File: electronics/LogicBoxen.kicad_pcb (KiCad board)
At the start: 2 copper layers, 50 x 35 mm, 47 parts, among them P1 Input, P2 Output, P3 Power, P4 L2, P5 L1, P6 OUT, Q1 Q_NMOS_DGS, SW1 DIPS_04, U1 4015, U2 4050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

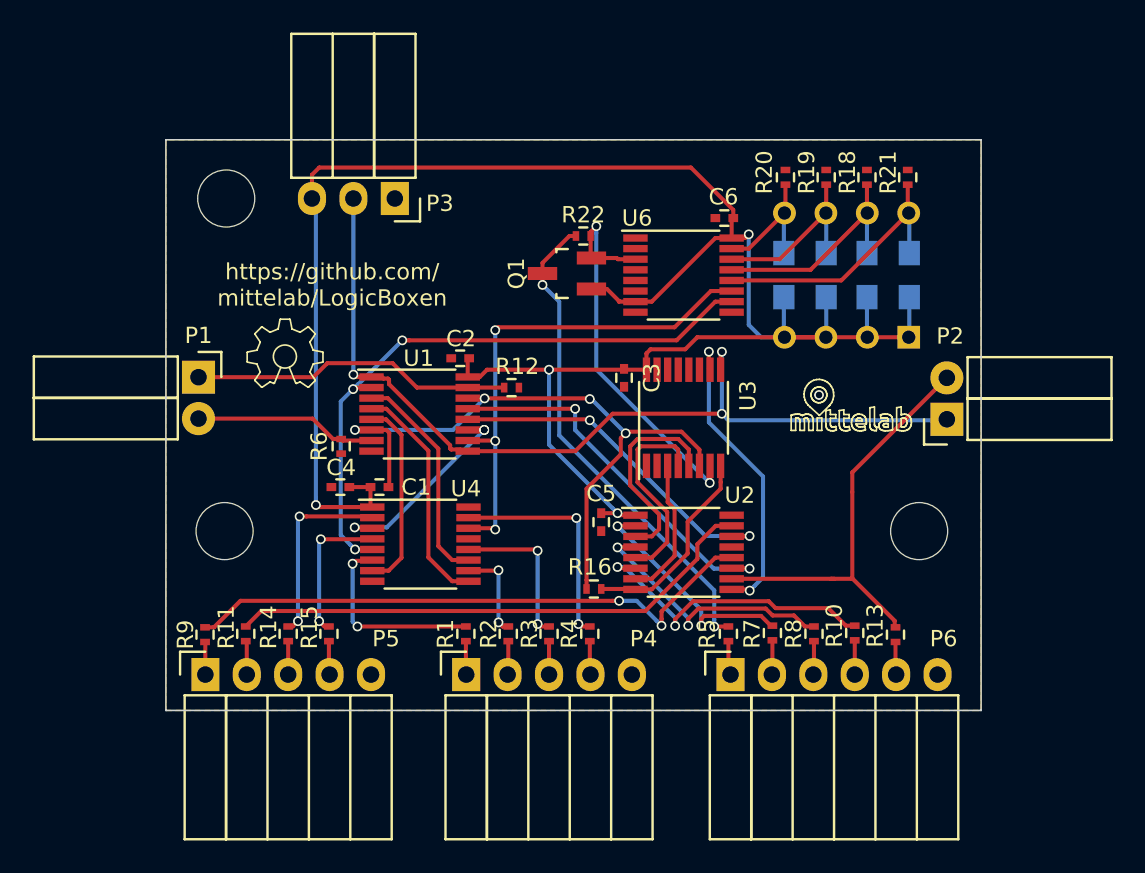
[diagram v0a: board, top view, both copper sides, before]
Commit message: Move vias away from pads, rearrange some tracks
Move R16 to a better place
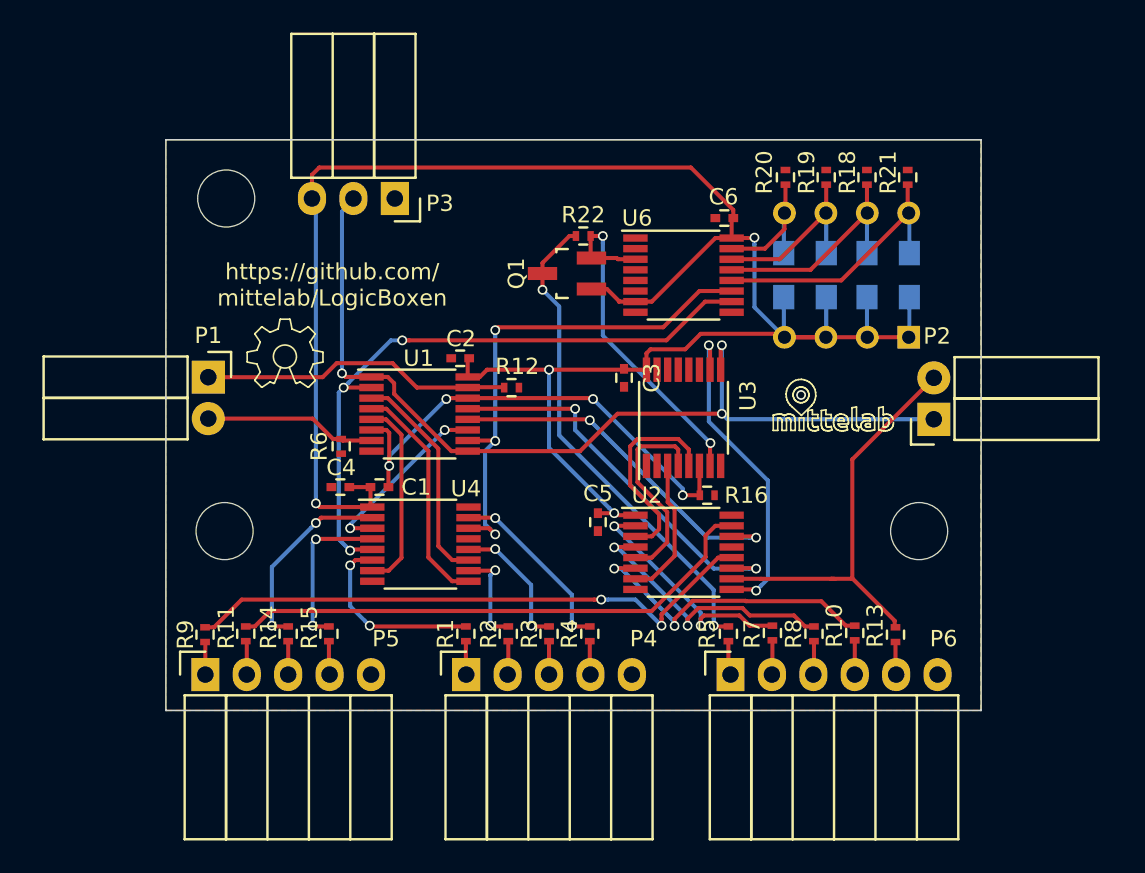
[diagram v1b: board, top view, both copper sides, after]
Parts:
- moved R16 9.02 mm to (57.2, 50.5)
- moved P2 0.80 mm to (71.1, 45.8)
- moved P1 0.60 mm to (26.6, 43.3)
- moved C5 0.20 mm to (50.5, 52.1)
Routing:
- net VSS: track 12.4 -> 0.06 mm
- net /reset: track 42.6 -> 30.3 mm
- net /out: track 24.6 -> 21.8 mm
- net Net-(R4-Pad1): track 13.9 -> 11.3 mm
- net /in_b: track 38.3 -> 39.6 mm
- net Net-(U2-Pad9): track 18.7 -> 19.9 mm
- net Net-(R3-Pad1): track 9.53 -> 8.38 mm
- net Net-(U1-Pad11): track 12.3 -> 11.2 mm, vias 3 -> 2
- net /clock: track 56.1 -> 57.1 mm
- net /in_a: track 31.1 -> 32.0 mm
- net Net-(R15-Pad1): track 8.97 -> 9.87 mm
- net VCC: track 130.6 -> 129.7 mm
- net Net-(U1-Pad12): track 21.4 -> 22.2 mm
- net Net-(U1-Pad13): track 23.3 -> 24.0 mm
- net Net-(P1-Pad2): track 11.2 -> 10.6 mm
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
